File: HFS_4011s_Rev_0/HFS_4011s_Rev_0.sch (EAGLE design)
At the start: 44 parts, among them IC1 CP2104, J1 2X06, J2 2X12, J3 1X02, Q1 mmbt2222, Q2 mmbt2222, Q3 MMUN2133LT1G, SW2 KMR2, U1 TPS61090RSAR, U2 MCP73831T-2ACI/OT, U3 LM3940, X2 ESP32_WROOM32_SKINNY, X4 20329

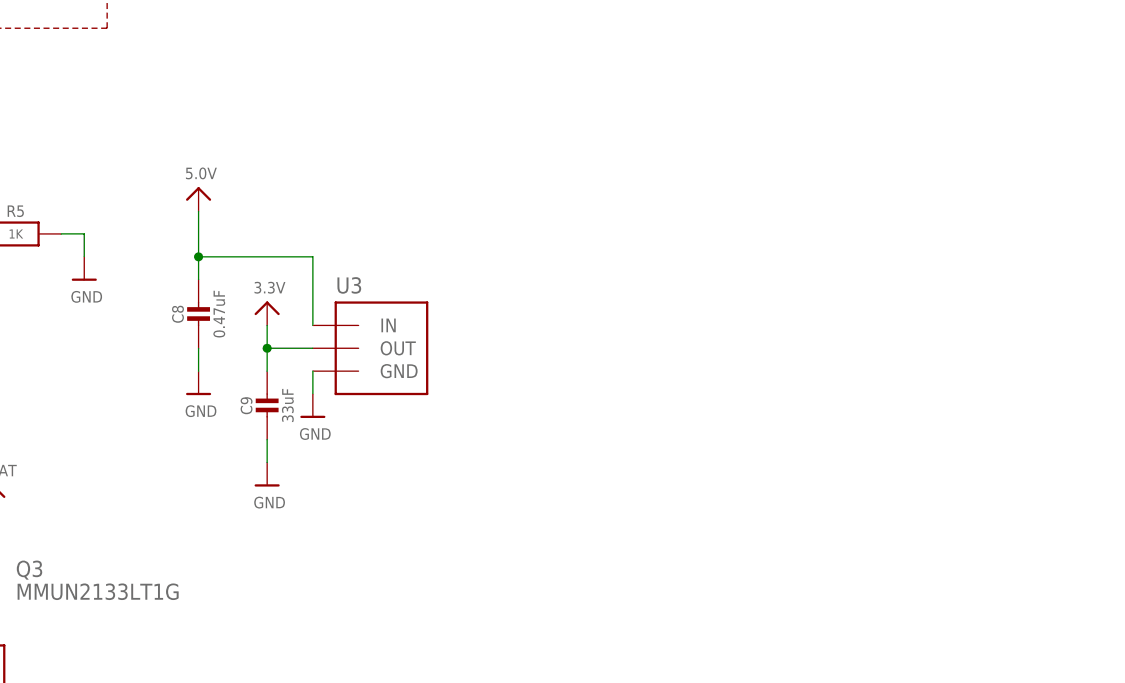
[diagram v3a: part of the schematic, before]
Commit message: Added in 3.3V buck converter and got rid of 3.3V LDO.
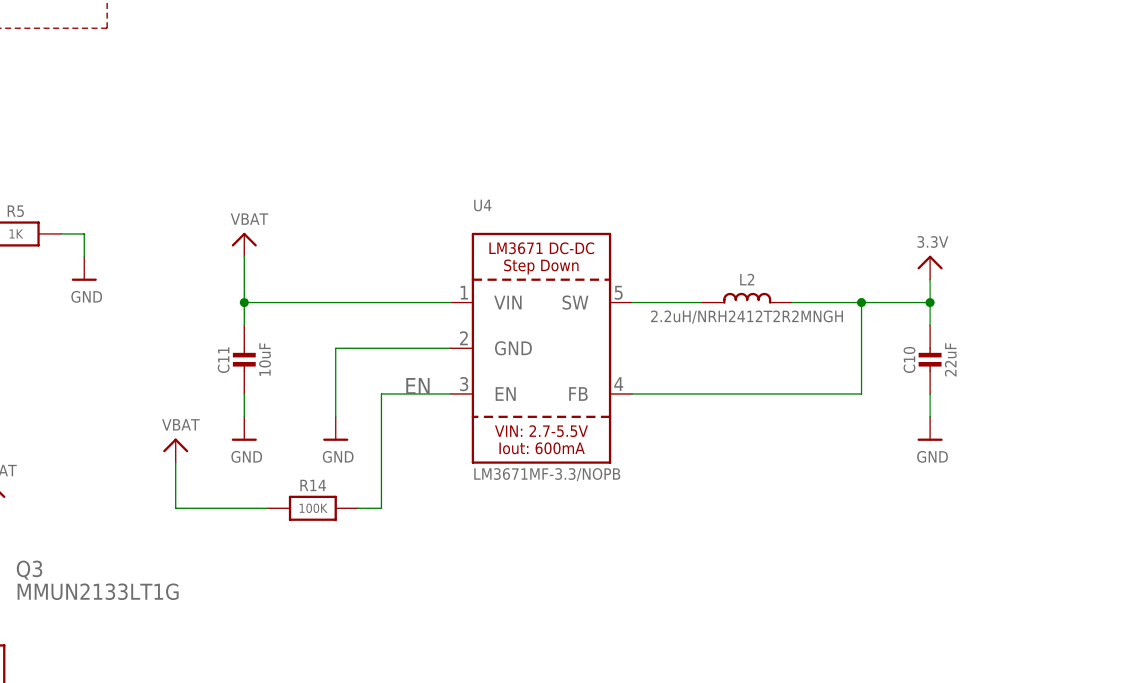
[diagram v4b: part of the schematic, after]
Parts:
- removed C8: 0.47uF, microbuilder:CAP_CERAMIC0603_NO
- removed C9: 33uF, microbuilder:CAP_CERAMIC0603_NO
- removed U3: LM3940, HFS4011sCustom:LM3940
- added C10: 22uF, microbuilder:CAP_CERAMIC0805-NOOUTLINE
- added C11: 10uF, microbuilder:CAP_CERAMIC0805-NOOUTLINE
- added L2: 2.2uH/NRH2412T2R2MNGH, microbuilder:INDUCTORNRH2412T
- added R14: 100K, microbuilder:RESISTOR0805_NOOUTLINE
- added U4: LM3671MF-3.3/NOPB, microbuilder:VREG_LM3671
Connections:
- new net EN: R14.2, U4.EN
- new net N$17: L2.1, U4.SW
- net 3.3V: now also C10.1, L2.2, U4.FB; no longer C9.1, U3.OUT
- net 5.0V: no longer C8.1, U3.IN
- net GND: now also C10.2, C11.2, U4.GND; no longer C8.2, C9.2, U3.GND
- net VBAT: now also C11.1, R14.1, U4.VIN
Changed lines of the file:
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@@
 <part name="Q3" library="transistor" deviceset="*-PNP_DRIVER-" device="SC59-BEC" technology="MUN2114T1" value="MMUN2133LT1G"/>
 <part name="J3" library="HFS4011sCustom" deviceset="1X02" device=""/>
-<part name="U3" library="HFS4011sCustom" deviceset="LM3940" device=""/>
-<part name="U$23" library="microbuilder" deviceset="GND" device=""/>
-<part name="U$25" library="microbuilder" deviceset="5.0V" device=""/>
-<part name="C8" library="microbuilder" deviceset="CAP_CERAMIC" device="0603_NO" value="0.47uF"/>
-<part name="C9" library="microbuilder" deviceset="CAP_CERAMIC" device="0603_NO" value="33uF"/>
-<part name="U$29" library="microbuilder" deviceset="GND" device=""/>
-<part name="U$30" library="microbuilder" deviceset="GND" device=""/>
-<part name="U$35" library="microbuilder" deviceset="3.3V" device=""/>
 <part name="D1" library="HFS4011sCustom" deviceset="SMAJ5.0CALFDKR-ND" device=""/>
 <part name="U$16" library="microbuilder" deviceset="GND" device=""/>
+<part name="U4" library="microbuilder" deviceset="VREG_LM3671" device="" value="LM3671MF-3.3/NOPB"/>
+<part name="L2" library="microbuilder" deviceset="INDUCTOR" device="NRH2412T" value="2.2uH/NRH2412T2R2MNGH"/>
+<part name="C10" library="microbuilder" deviceset="CAP_CERAMIC" device="0805-NOOUTLINE" value="22uF"/>
+<part name="U$28" library="microbuilder" deviceset="GND" device=""/>
+<part name="U$36" library="microbuilder" deviceset="3.3V" device=""/>
+<part name="C11" library="microbuilder" deviceset="CAP_CERAMIC" device="0805-NOOUTLINE" value="10uF"/>
+<part name="U$38" library="microbuilder" deviceset="GND" device=""/>
+<part name="U$43" library="microbuilder" deviceset="GND" device=""/>
+<part name="R14" library="microbuilder" deviceset="RESISTOR" device="0805_NOOUTLINE" value="100K"/>
+<part name="U$23" library="microbuilder" deviceset="VBAT" device=""/>
+<part name="U$25" library="microbuilder" deviceset="VBAT" device=""/>
 </parts>
 <sheets>
@@
 </instance>
 <instance part="J3" gate="G$1" x="17.78" y="76.2" rot="R90"/>
-<instance part="U3" gate="G$1" x="177.8" y="78.74"/>
-<instance part="U$23" gate="G$1" x="172.72" y="71.12"/>
-<instance part="U$25" gate="G$1" x="160.02" y="96.52"/>
-<instance part="C8" gate="G$1" x="160.02" y="81.28"/>
-<instance part="C9" gate="G$1" x="167.64" y="71.12"/>
-<instance part="U$29" gate="G$1" x="160.02" y="73.66"/>
-<instance part="U$30" gate="G$1" x="167.64" y="63.5"/>
-<instance part="U$35" gate="G$1" x="167.64" y="83.82"/>
 <instance part="D1" gate="G$1" x="22.86" y="66.04" rot="R90"/>
 <instance part="U$16" gate="G$1" x="22.86" y="55.88"/>
+<instance part="U4" gate="G$1" x="198.12" y="78.74"/>
+<instance part="L2" gate="G$1" x="220.98" y="83.82"/>
+<instance part="C10" gate="G$1" x="241.3" y="76.2"/>
+<instance part="U$28" gate="G$1" x="241.3" y="68.58"/>
+<instance part="U$36" gate="G$1" x="241.3" y="88.9"/>
+<instance part="C11" gate="G$1" x="165.1" y="76.2"/>
+<instance part="U$38" gate="G$1" x="165.1" y="68.58"/>
+<instance part="U$43" gate="G$1" x="175.26" y="68.58"/>
+<instance part="R14" gate="G$1" x="172.72" y="60.96"/>
+<instance part="U$23" gate="G$1" x="165.1" y="91.44"/>
+<instance part="U$25" gate="G$1" x="157.48" y="68.58"/>
 </instances>
 <busses>
@@
 </segment>
 <segment>
-<pinref part="C8" gate="G$1" pin="2"/>
-<pinref part="U$29" gate="G$1" pin="GND"/>
-<wire x1="160.02" y1="78.74" x2="160.02" y2="76.2" width="0.1524" layer="91"/>
-</segment>
-<segment>
-<pinref part="U$23" gate="G$1" pin="GND"/>
-<pinref part="U3" gate="G$1" pin="GND"/>
-<wire x1="172.72" y1="73.66" x2="172.72" y2="76.2" width="0.1524" layer="91"/>
-</segment>
-<segment>
-<pinref part="U$30" gate="G$1" pin="GND"/>
-<pinref part="C9" gate="G$1" pin="2"/>
-<wire x1="167.64" y1="66.04" x2="167.64" y2="68.58" width="0.1524" layer="91"/>
-</segment>
-<segment>
 <pinref part="D1" gate="G$1" pin="A"/>
 <pinref part="U$16" gate="G$1" pin="GND"/>
 <wire x1="22.86" y1="63.5" x2="22.86" y2="58.42" width="0.1524" layer="91"/>
+</segment>
+<segment>
+<pinref part="C10" gate="G$1" pin="2"/>
+<pinref part="U$28" gate="G$1" pin="GND"/>
+<wire x1="241.3" y1="73.66" x2="241.3" y2="71.12" width="0.1524" layer="91"/>
+</segment>
+<segment>
+<pinref part="C11" gate="G$1" pin="2"/>
+<pinref part="U$38" gate="G$1" pin="GND"/>
+<wire x1="165.1" y1="73.66" x2="165.1" y2="71.12" width="0.1524" layer="91"/>
+</segment>
+<segment>
+<pinref part="U4" gate="G$1" pin="GND"/>
+<pinref part="U$43" gate="G$1" pin="GND"/>
+<wire x1="187.96" y1="78.74" x2="175.26" y2="78.74" width="0.1524" layer="91"/>
+<wire x1="175.26" y1="78.74" x2="175.26" y2="71.12" width="0.1524" layer="91"/>
 </segment>
 </net>
@@
 <pinref part="Q3" gate="G$1" pin="E"/>
 </segment>
+<segment>
+<pinref part="R14" gate="G$1" pin="1"/>
+<wire x1="167.64" y1="60.96" x2="157.48" y2="60.96" width="0.1524" layer="91"/>
+<pinref part="U$25" gate="G$1" pin="VBAT"/>
+<wire x1="157.48" y1="66.04" x2="157.48" y2="60.96" width="0.1524" layer="91"/>
+</segment>
+<segment>
+<pinref part="U4" gate="G$1" pin="VIN"/>
+<wire x1="187.96" y1="83.82" x2="165.1" y2="83.82" width="0.1524" layer="91"/>
+<pinref part="C11" gate="G$1" pin="1"/>
+<wire x1="165.1" y1="83.82" x2="165.1" y2="81.28" width="0.1524" layer="91"/>
+<pinref part="U$23" gate="G$1" pin="VBAT"/>
+<wire x1="165.1" y1="88.9" x2="165.1" y2="83.82" width="0.1524" layer="91"/>
+<junction x="165.1" y="83.82"/>
+</segment>
 </net>
 <net name="3.3V" class="0">
@@
 </segment>
 <segment>
-<pinref part="C9" gate="G$1" pin="1"/>
-<pinref part="U3" gate="G$1" pin="OUT"/>
-<wire x1="167.64" y1="78.74" x2="167.64" y2="76.2" width="0.1524" layer="91"/>
-<wire x1="172.72" y1="78.74" x2="167.64" y2="78.74" width="0.1524" layer="91"/>
-<pinref part="U$35" gate="G$1" pin="3.3V"/>
-<wire x1="167.64" y1="81.28" x2="167.64" y2="78.74" width="0.1524" layer="91"/>
-<junction x="167.64" y="78.74"/>
+<pinref part="U4" gate="G$1" pin="FB"/>
+<wire x1="208.28" y1="73.66" x2="233.68" y2="73.66" width="0.1524" layer="91"/>
+<wire x1="233.68" y1="73.66" x2="233.68" y2="83.82" width="0.1524" layer="91"/>
+<pinref part="L2" gate="G$1" pin="2"/>
+<wire x1="233.68" y1="83.82" x2="226.06" y2="83.82" width="0.1524" layer="91"/>
+<pinref part="C10" gate="G$1" pin="1"/>
+<wire x1="233.68" y1="83.82" x2="241.3" y2="83.82" width="0.1524" layer="91"/>
+<wire x1="241.3" y1="83.82" x2="241.3" y2="81.28" width="0.1524" layer="91"/>
+<junction x="233.68" y="83.82"/>
+<pinref part="U$36" gate="G$1" pin="3.3V"/>
+<wire x1="241.3" y1="83.82" x2="241.3" y2="86.36" width="0.1524" layer="91"/>
+<junction x="241.3" y="83.82"/>
 </segment>
 </net>
@@
 <pinref part="C7" gate="G$1" pin="+"/>
 </segment>
-<segment>
-<pinref part="U$25" gate="G$1" pin="5.0V"/>
-<pinref part="C8" gate="G$1" pin="1"/>
-<wire x1="160.02" y1="93.98" x2="160.02" y2="88.9" width="0.1524" layer="91"/>
-<pinref part="U3" gate="G$1" pin="IN"/>
-<wire x1="160.02" y1="88.9" x2="160.02" y2="86.36" width="0.1524" layer="91"/>
-<wire x1="160.02" y1="88.9" x2="172.72" y2="88.9" width="0.1524" layer="91"/>
-<wire x1="172.72" y1="88.9" x2="172.72" y2="81.28" width="0.1524" layer="91"/>
-<junction x="160.02" y="88.9"/>
-</segment>
 </net>
 <net name="N$10" class="0">
@@
 </segment>
 </net>
+<net name="N$17" class="0">
+<segment>
+<pinref part="L2" gate="G$1" pin="1"/>
+<pinref part="U4" gate="G$1" pin="SW"/>
+<wire x1="215.9" y1="83.82" x2="208.28" y2="83.82" width="0.1524" layer="91"/>
+</segment>
+</net>
+<net name="EN" class="0">
+<segment>
+<pinref part="U4" gate="G$1" pin="EN"/>
+<wire x1="187.96" y1="73.66" x2="180.34" y2="73.66" width="0.1524" layer="91"/>
+<wire x1="180.34" y1="73.66" x2="180.34" y2="60.96" width="0.1524" layer="91"/>
+<pinref part="R14" gate="G$1" pin="2"/>
+<wire x1="180.34" y1="60.96" x2="177.8" y2="60.96" width="0.1524" layer="91"/>
+<label x="182.88" y="73.66" size="1.778" layer="95"/>
+</segment>
+</net>

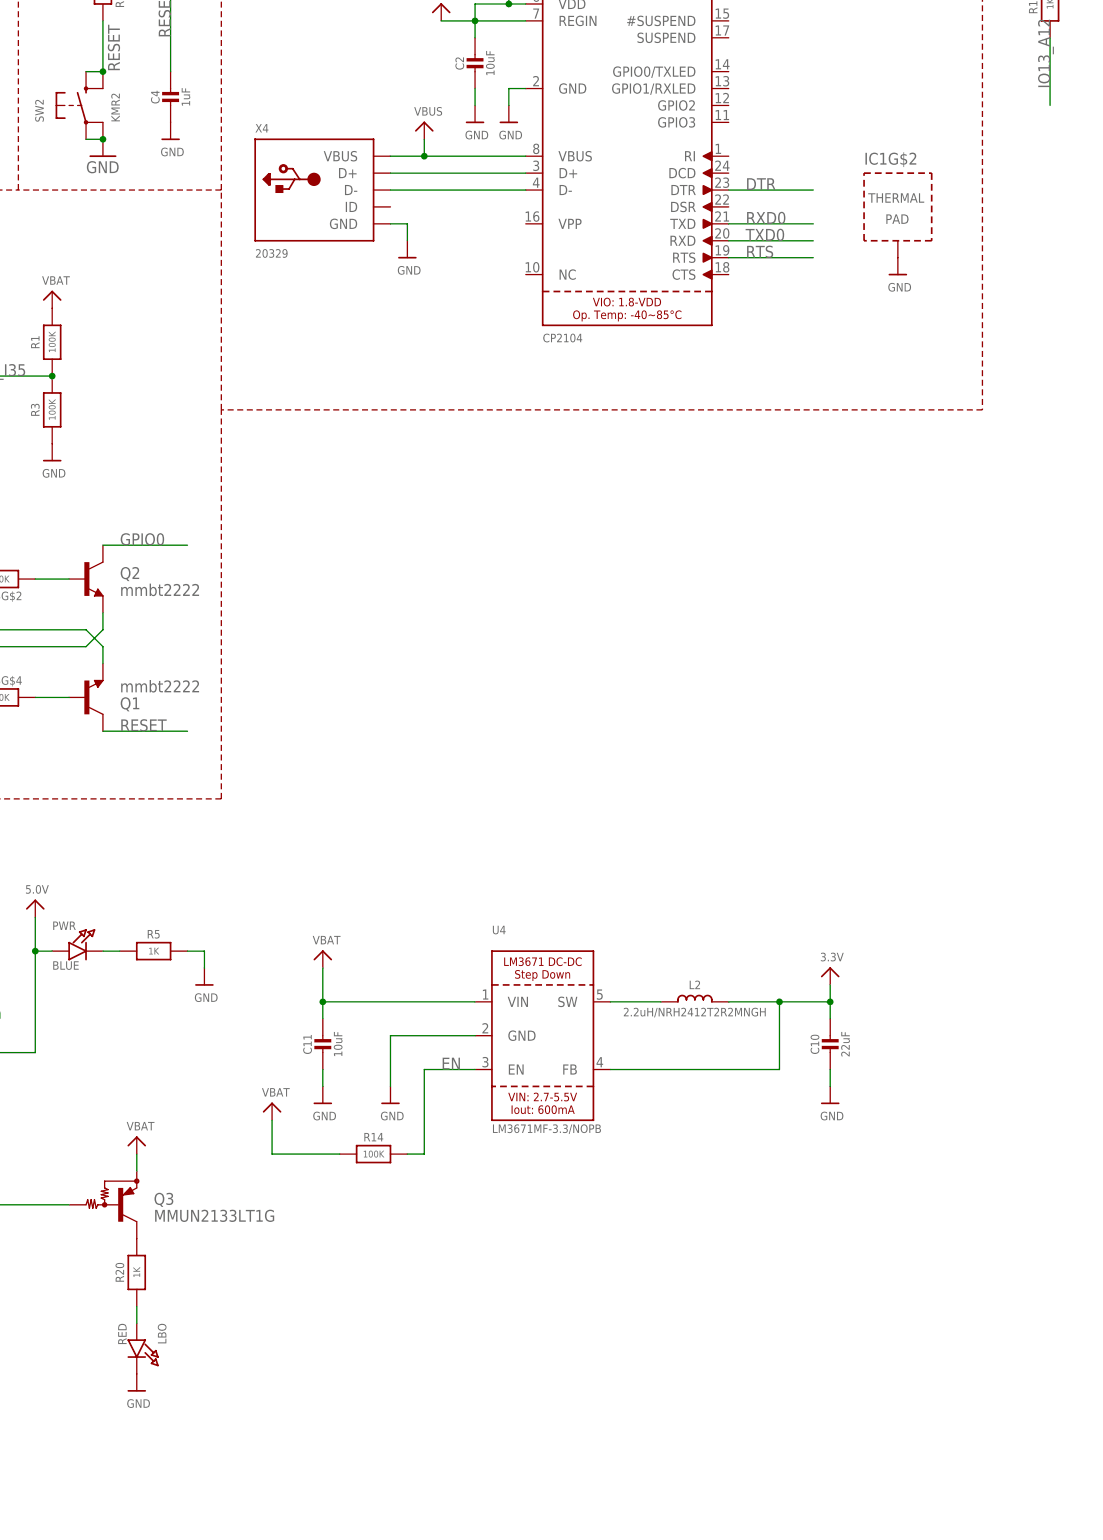
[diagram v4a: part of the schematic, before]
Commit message: Added in DAC
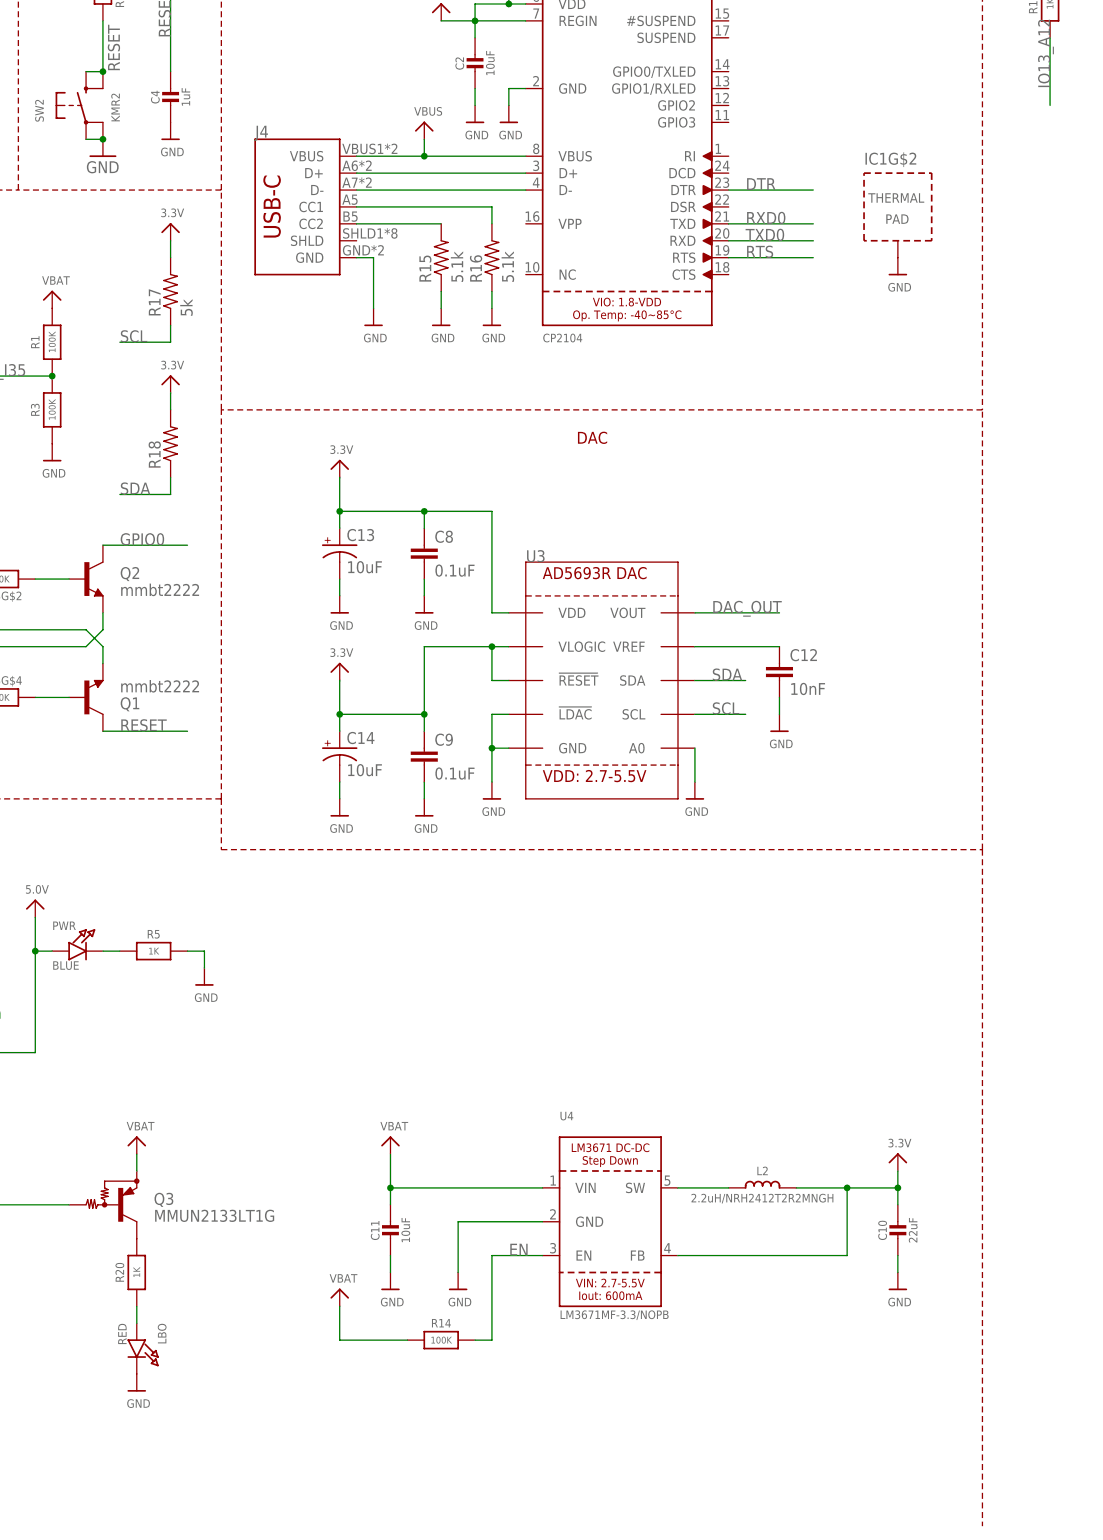
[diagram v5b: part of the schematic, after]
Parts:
- removed X4: 20329, microbuilder:USB_MICRO_20329_V2
- added C12: 10nF, rcl:C-EUC0603
- added C13, C14: 10uF, SparkFun-Retired:10UF-TANT
- added C8, C9: 0.1uF, rcl:C-EUC0603
- added J4: (no value), SparkFun-Connectors:USB_C16PIN
- added R15, R16: 5.1k, rcl:R-US_R0603
- added R17: 5k, rcl:R-US_R0603
- added R18: (no value), rcl:R-US_R0603
- added U3: AD5693R, HFS4011sCustom:AD5693R
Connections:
- new net DAC_OUT: U3.VOUT
- new net N$18: J4.CC1, R16.2
- new net N$19: J4.CC2, R15.2
- new net N$20: C12.1, U3.VREF
- net 3.3V: now also C13.+, C14.+, C8.1, C9.1, R17.2, R18.2, U3.!RESET!, U3.VDD, U3.VLOGIC
- net GND: now also C12.2, C13.-, C14.-, C8.2, C9.2, J4.GND, R15.1, R16.1, U3.!LDAC!, U3.A0, U3.GND; no longer X4.GND
- net N$2: now also J4.D+; no longer X4.D+
- net N$6: now also J4.D-; no longer X4.D-
- net SCL: now also R17.1, U3.SCL
- net SDA: now also R18.1, U3.SDA
- net VBUS: now also J4.VBUS; no longer X4.VBUS
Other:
- note added: "DAC"
- moved on the sheet: C10, C11, L2, R14, U4
